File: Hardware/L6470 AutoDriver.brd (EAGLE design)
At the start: 73.7 x 49.5 mm, 35 parts, among them U1 L6470

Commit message: Production ready
created 4 board panel; added fiducials
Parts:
- added FID1, FID2: FIDUCIALUFIDUCIAL, SparkFun-Aesthetics:MICRO-FIDUCIAL
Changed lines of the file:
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@@
 <setting verticaltext="up"/>
 </settings>
-<grid distance="0.05" unitdist="inch" unit="inch" style="lines" multiple="1" display="yes" altdistance="0.005" altunitdist="inch" altunit="inch"/>
+<grid distance="0.05" unitdist="inch" unit="inch" style="lines" multiple="1" display="yes" altdistance="0.01" altunitdist="inch" altunit="inch"/>
 <layers>
 <layer number="1" name="Top" color="4" fill="1" visible="yes" active="yes"/>
-<layer number="2" name="Route2" color="1" fill="3" visible="no" active="yes"/>
-<layer number="15" name="Route15" color="4" fill="6" visible="no" active="yes"/>
+<layer number="2" name="Route2" color="1" fill="3" visible="yes" active="yes"/>
+<layer number="15" name="Route15" color="4" fill="6" visible="yes" active="yes"/>
 <layer number="16" name="Bottom" color="1" fill="1" visible="yes" active="yes"/>
 <layer number="17" name="Pads" color="2" fill="1" visible="yes" active="yes"/>
@@
 <layer number="19" name="Unrouted" color="6" fill="1" visible="yes" active="yes"/>
 <layer number="20" name="Dimension" color="6" fill="1" visible="yes" active="yes"/>
-<layer number="21" name="tPlace" color="16" fill="1" visible="yes" active="yes"/>
-<layer number="22" name="bPlace" color="14" fill="1" visible="yes" active="yes"/>
+<layer number="21" name="tPlace" color="6" fill="1" visible="yes" active="yes"/>
+<layer number="22" name="bPlace" color="6" fill="1" visible="yes" active="yes"/>
 <layer number="23" name="tOrigins" color="15" fill="1" visible="yes" active="yes"/>
 <layer number="24" name="bOrigins" color="15" fill="1" visible="yes" active="yes"/>
-<layer number="25" name="tNames" color="7" fill="1" visible="no" active="yes"/>
-<layer number="26" name="bNames" color="7" fill="1" visible="no" active="yes"/>
-<layer number="27" name="tValues" color="7" fill="1" visible="no" active="yes"/>
-<layer number="28" name="bValues" color="7" fill="1" visible="no" active="yes"/>
-<layer number="29" name="tStop" color="7" fill="3" visible="no" active="yes"/>
-<layer number="30" name="bStop" color="7" fill="6" visible="no" active="yes"/>
-<layer number="31" name="tCream" color="7" fill="4" visible="no" active="yes"/>
-<layer number="32" name="bCream" color="7" fill="5" visible="no" active="yes"/>
-<layer number="39" name="tKeepout" color="4" fill="11" visible="no" active="yes"/>
-<layer number="40" name="bKeepout" color="1" fill="11" visible="no" active="yes"/>
-<layer number="41" name="tRestrict" color="4" fill="10" visible="no" active="yes"/>
-<layer number="42" name="bRestrict" color="1" fill="10" visible="no" active="yes"/>
-<layer number="43" name="vRestrict" color="2" fill="10" visible="no" active="yes"/>
-<layer number="44" name="Drills" color="7" fill="1" visible="no" active="yes"/>
+<layer number="25" name="tNames" color="7" fill="1" visible="yes" active="yes"/>
+<layer number="26" name="bNames" color="7" fill="1" visible="yes" active="yes"/>
+<layer number="27" name="tValues" color="7" fill="1" visible="yes" active="yes"/>
+<layer number="28" name="bValues" color="7" fill="1" visible="yes" active="yes"/>
+<layer number="29" name="tStop" color="7" fill="3" visible="yes" active="yes"/>
+<layer number="30" name="bStop" color="7" fill="6" visible="yes" active="yes"/>
+<layer number="31" name="tCream" color="7" fill="4" visible="yes" active="yes"/>
+<layer number="32" name="bCream" color="7" fill="5" visible="yes" active="yes"/>
+<layer number="39" name="tKeepout" color="4" fill="11" visible="yes" active="yes"/>
+<layer number="40" name="bKeepout" color="1" fill="11" visible="yes" active="yes"/>
+<layer number="41" name="tRestrict" color="4" fill="10" visible="yes" active="yes"/>
+<layer number="42" name="bRestrict" color="1" fill="10" visible="yes" active="yes"/>
+<layer number="43" name="vRestrict" color="2" fill="10" visible="yes" active="yes"/>
+<layer number="44" name="Drills" color="7" fill="1" visible="yes" active="yes"/>
 <layer number="45" name="Holes" color="7" fill="1" visible="yes" active="yes"/>
-<layer number="46" name="Milling" color="3" fill="1" visible="no" active="yes"/>
+<layer number="46" name="Milling" color="3" fill="1" visible="yes" active="yes"/>
 <layer number="51" name="tDocu" color="6" fill="1" visible="yes" active="yes"/>
-<layer number="52" name="bDocu" color="7" fill="1" visible="no" active="yes"/>
+<layer number="52" name="bDocu" color="7" fill="1" visible="yes" active="yes"/>
 <layer number="3" name="Route3" color="4" fill="3" visible="no" active="no"/>
 <layer number="4" name="Route4" color="1" fill="4" visible="no" active="no"/>
@@
 <element name="SJ2" library="SparkFun-Passives" package="2PT_GND_TIE" value="2PT_GND_TIE" x="39.37" y="21.59"/>
 <element name="U$4" library="SparkFun-Aesthetics" package="FOUR_LAYER_WARNING" value="FOUR_LAYER_WARNING" x="0" y="-2.54"/>
+<element name="FID1" library="SparkFun-Aesthetics" package="MICRO-FIDUCIAL" value="FIDUCIALUFIDUCIAL" x="67.31" y="2.54"/>
+<element name="FID2" library="SparkFun-Aesthetics" package="MICRO-FIDUCIAL" value="FIDUCIALUFIDUCIAL" x="1.27" y="43.18"/>
 </elements>
 <signals>

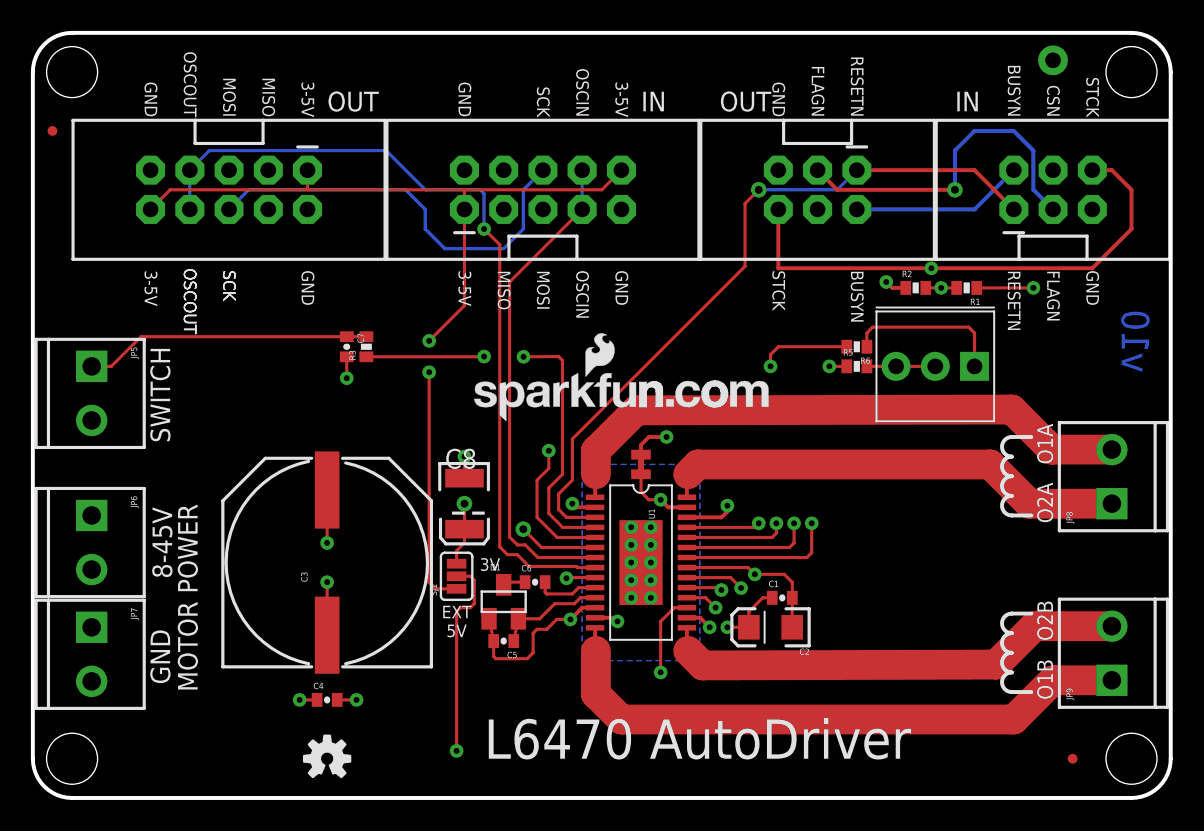
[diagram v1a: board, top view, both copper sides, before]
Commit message: 0603 update, Sch work, cap change
Updated res/caps to 0603
large cap updated to smaller silk/pad size
jumper indicator added, OSHW logo upgraded
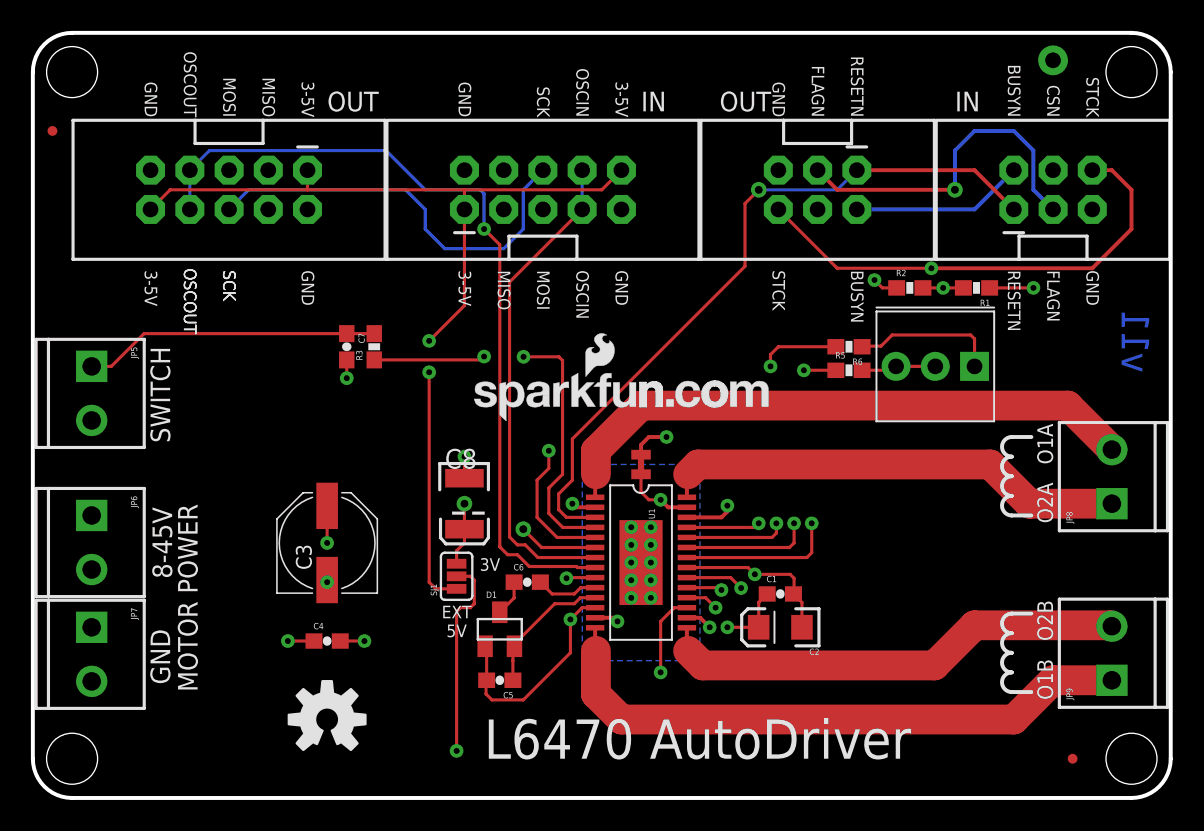
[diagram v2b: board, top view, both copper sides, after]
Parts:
- C1, C4, C5, C6, C7: device SparkFun-Capacitors:0402-CAP -> SparkFun-Capacitors:0603-CAP
- C3: device SparkFun-Capacitors:PANASONIC_H13 -> SparkFun-Capacitors:PANASONIC_D
- LOGO1: value OSHW-LOGOS -> OSHW-LOGOM; device SparkFun:OSHW-LOGO-S -> SparkFun-Aesthetics:OSHW-LOGO-M
- R1, R2, R3, R5, R6: device SparkFun-Resistors:0402-RES -> SparkFun-Resistors:0603-RES
- moved FRAME1 10.2 mm to (6.35, -20.3)
- moved U$4 10.2 mm to (-5.08, -11.4)
- moved C4 3.81 mm to (19.1, 10.2)
- moved C5 2.55 mm to (30.2, 7.62)
- moved LOGO1 2.54 mm to (19.1, 5.08)
- moved D1 1.80 mm to (30.2, 10.9)
- moved C3 1.27 mm to (19.1, 16.5)
- moved R1 0.64 mm to (61.1, 33.0)
- moved C2 0.63 mm to (48.4, 11.0)
- moved R5 0.57 mm to (52.8, 27.7)
- moved C6 0.51 mm to (32.0, 14.0)
- moved R6 0.51 mm to (52.8, 29.2)
- moved R3 0.51 mm to (22.1, 29.2)
- moved R2 0.38 mm to (56.8, 33.0)
- moved C1 0.28 mm to (48.4, 13.2)
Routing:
- net PGND: track 11.4 -> 8.41 mm
- net N$9: track 7.01 -> 9.00 mm
- net STCK: track 73.2 -> 71.2 mm
- net VS: track 38.4 -> 40.1 mm
- net GND: track 18.4 -> 19.7 mm
- net FLAGN: track 74.2 -> 75.2 mm
- net N$8: track 1.45 -> 2.33 mm
- net N$11: track 10.3 -> 9.48 mm
- net BUSYN: track 61.7 -> 60.9 mm
- net VLOGIC: track 91.3 -> 92.1 mm
- net N$6: track 18.6 -> 19.2 mm
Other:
- board text added: "Revised by: Patrick Alberts"
- board text added: "v11"
- board text removed: "v10"

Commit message: Moved via
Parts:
- moved C4 0.63 mm to (19.1, 9.53)
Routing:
- net PGND: track 8.41 -> 10.8 mm
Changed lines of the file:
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@@
 <attribute name="VALUE" value="10nF" x="30.226" y="7.62" size="1.778" layer="27" rot="R180" display="off"/>
 </element>
-<element name="C4" library="SparkFun-Capacitors" package="0603-CAP" value="0.22uF" x="19.05" y="10.16">
-<attribute name="PROD_ID" value="CAP-09885" x="19.05" y="10.16" size="1.778" layer="27" display="off"/>
-<attribute name="VALUE" value="0.22uF" x="19.05" y="10.16" size="1.778" layer="27" display="off"/>
+<element name="C4" library="SparkFun-Capacitors" package="0603-CAP" value="0.22uF" x="19.05" y="9.525">
+<attribute name="PROD_ID" value="CAP-09885" x="19.05" y="9.525" size="1.778" layer="27" display="off"/>
+<attribute name="VALUE" value="0.22uF" x="19.05" y="9.525" size="1.778" layer="27" display="off"/>
 </element>
 <element name="C3" library="SparkFun-Capacitors" package="PANASONIC_D" value="100uF" x="19.05" y="16.51" rot="R90"/>
@@
 <wire x1="35.444" y1="12.965" x2="35.052" y2="12.573" width="0.2032" layer="1"/>
 <wire x1="35.052" y1="12.573" x2="33.782" y2="12.573" width="0.2032" layer="1"/>
-<wire x1="31.076" y1="7.62" x2="31.076" y2="8.89" width="0.2032" layer="1"/>
-<wire x1="31.076" y1="8.89" x2="31.076" y2="9.722" width="0.2032" layer="1"/>
 <wire x1="31.076" y1="9.722" x2="31.176" y2="9.822" width="0.2032" layer="1"/>
 <wire x1="33.782" y1="12.573" x2="31.076" y2="9.867" width="0.2032" layer="1"/>
 <wire x1="31.076" y1="9.867" x2="31.076" y2="9.722" width="0.2032" layer="1"/>
+<wire x1="31.076" y1="9.722" x2="31.076" y2="7.62" width="0.2032" layer="1"/>
 </signal>
 <signal name="OUT1A">
@@
 <wire x1="19.05" y1="18.91" x2="19.05" y2="16.51" width="0.2032" layer="1"/>
 <via x="19.05" y="16.51" extent="1-16" drill="0.381"/>
-<wire x1="18.2" y1="10.16" x2="16.51" y2="10.16" width="0.2032" layer="1"/>
-<via x="16.51" y="10.16" extent="1-16" drill="0.381"/>
+<wire x1="18.2" y1="9.525" x2="16.51" y2="9.525" width="0.2032" layer="1"/>
+<via x="16.51" y="9.525" extent="1-16" drill="0.381"/>
 <wire x1="29.376" y1="7.62" x2="29.376" y2="9.722" width="0.2032" layer="1"/>
 <wire x1="29.376" y1="9.722" x2="29.276" y2="9.822" width="0.2032" layer="1"/>
@@
 <via x="38.735" y="17.526" extent="1-16" drill="0.381"/>
 <wire x1="39.37" y1="15.24" x2="40.005" y2="15.24" width="0.2032" layer="1"/>
-<wire x1="19.9" y1="10.16" x2="21.463" y2="10.16" width="0.2032" layer="1"/>
-<via x="21.463" y="10.16" extent="1-16" drill="0.381"/>
-<wire x1="19.05" y1="14.11" x2="19.05" y2="13.97" width="0.2032" layer="1"/>
-<via x="19.05" y="13.97" extent="1-16" drill="0.381"/>
+<wire x1="19.9" y1="9.525" x2="21.463" y2="9.525" width="0.2032" layer="1"/>
+<via x="21.463" y="9.525" extent="1-16" drill="0.381"/>
+<wire x1="19.05" y1="14.11" x2="19.05" y2="11.557" width="0.2032" layer="1"/>
+<via x="19.05" y="11.557" extent="1-16" drill="0.381"/>
 <polygon width="0.2032" layer="16" isolate="0.3048">
 <vertex x="35.56" y="8.89"/>
